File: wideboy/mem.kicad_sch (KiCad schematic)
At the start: 9 parts, among them U10 LH28F320BJE-PTTL90, U11 µPD45128163G5-A75-9Jf, U9 XC17S20LPC

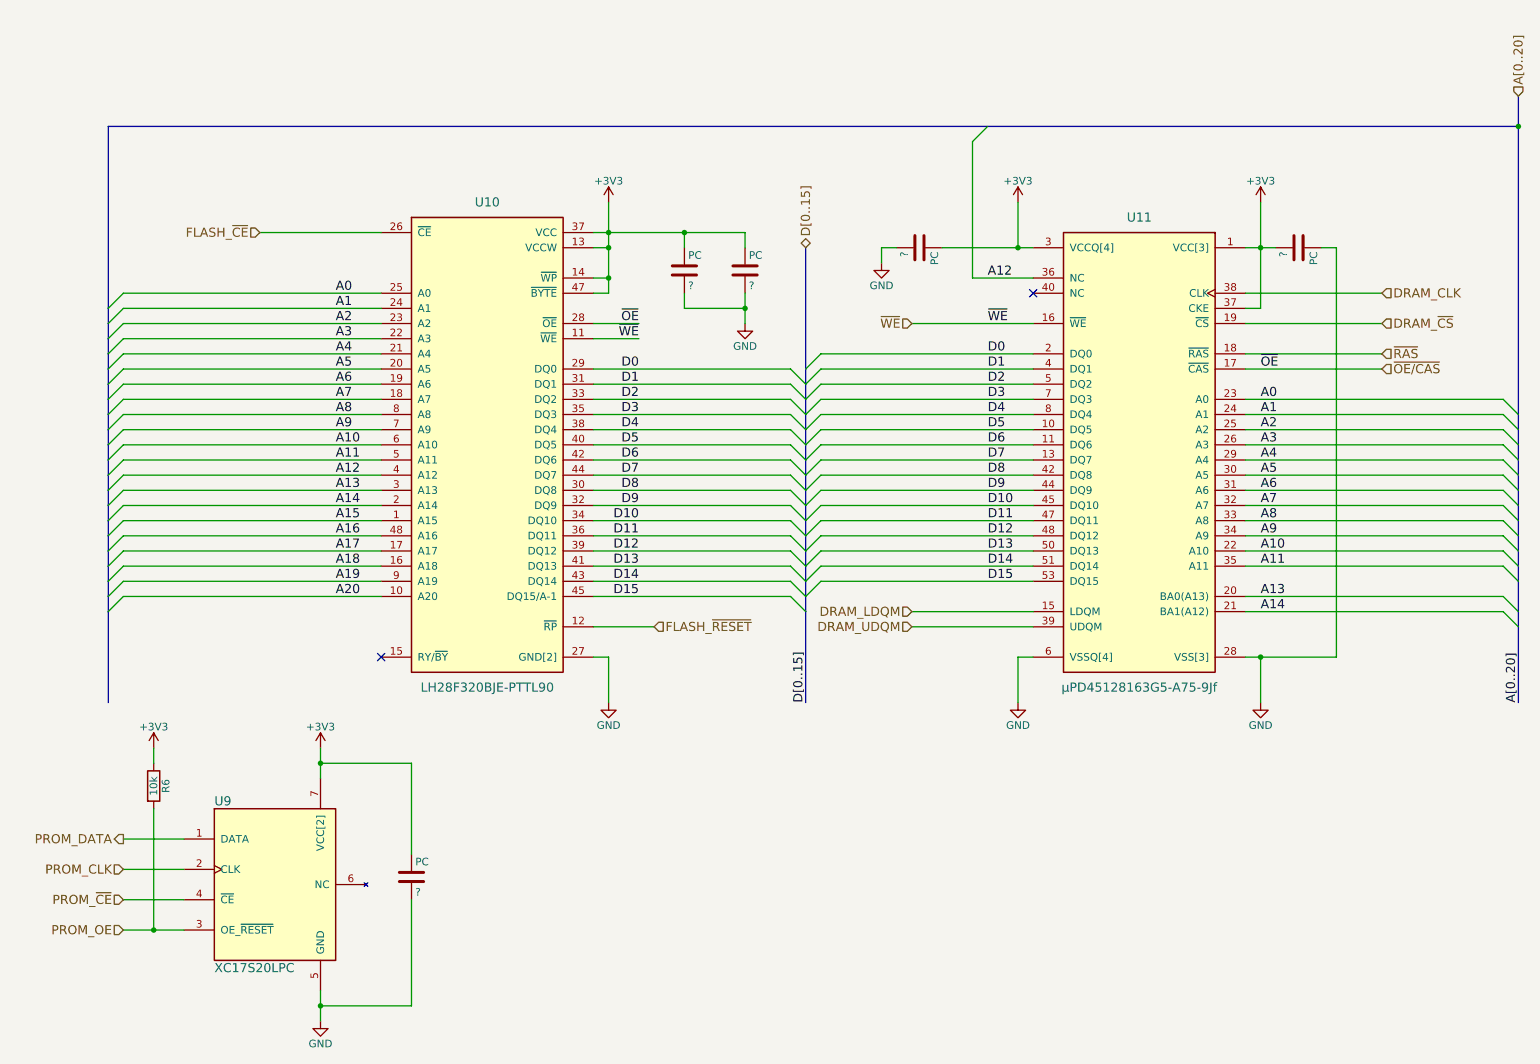
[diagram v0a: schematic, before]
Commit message: Add values for capacitors and diodes
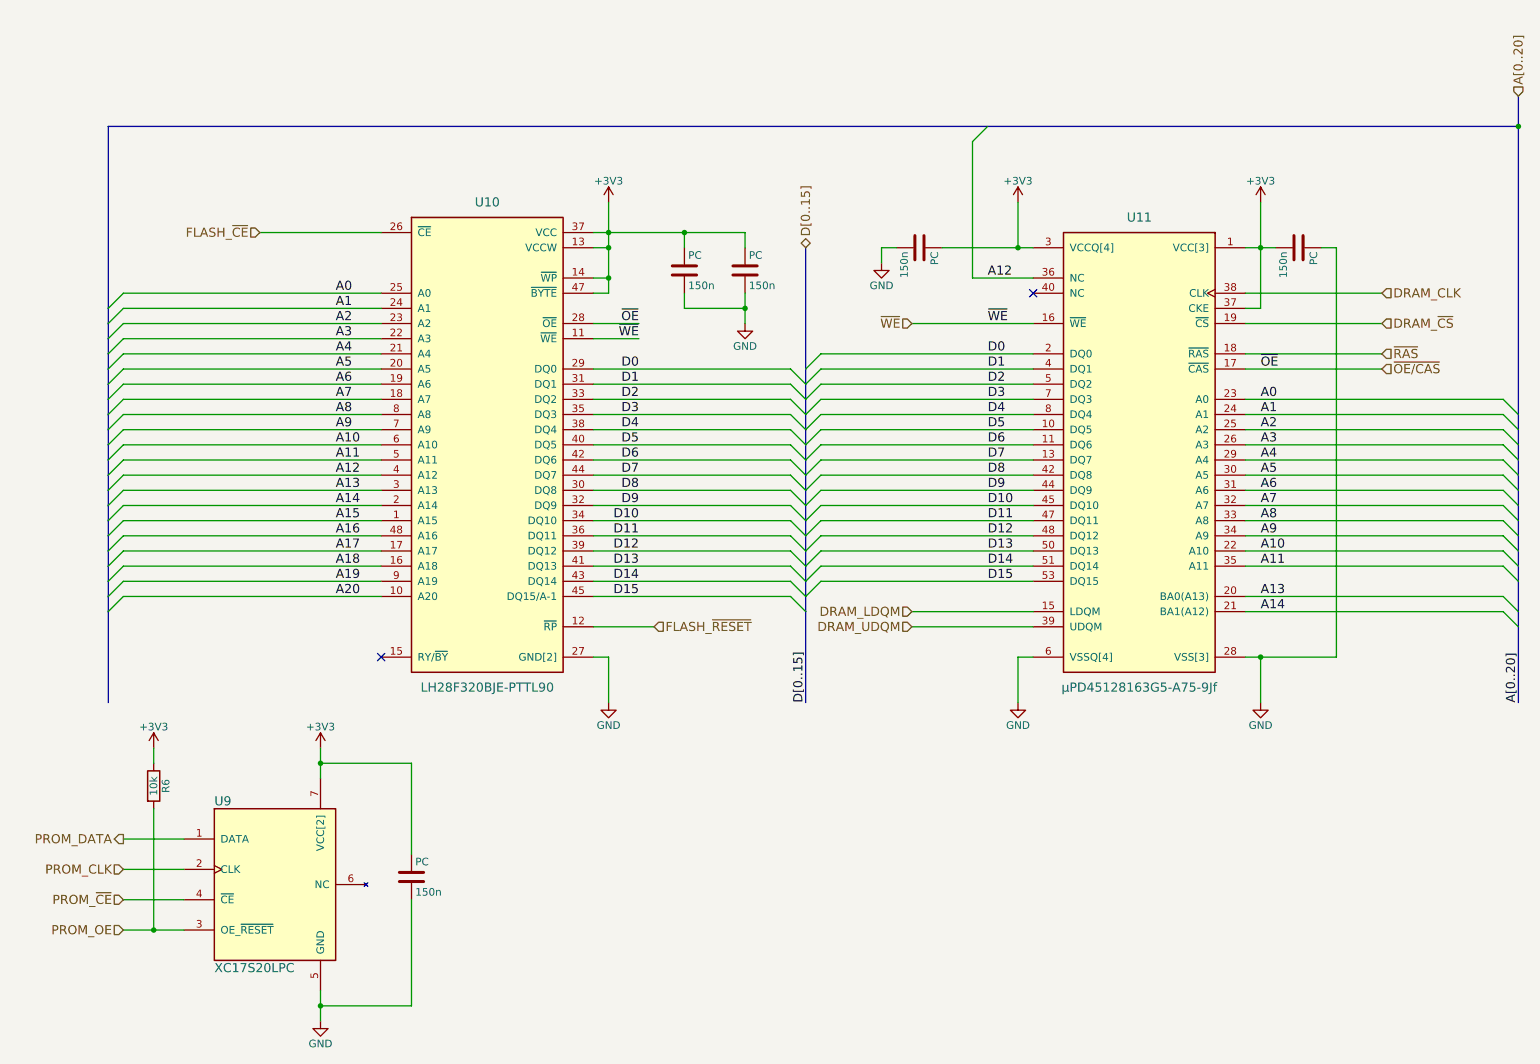
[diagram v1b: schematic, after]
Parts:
- PC: value ? -> 150n
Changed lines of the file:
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@@
 	(title_block
 		(title "Wide-Boy64 AGB")
-		(date "2024-06-20")
-		(rev "2")
+		(date "2024-09-22")
+		(rev "3")
 		(company "CC-BY-SA-4.0 Michael Singer")
 		(comment 1 "https://github.com/msinger/wideboy/")
@@
 			)
 		)
-		(property "Value" "?"
+		(property "Value" "150n"
 			(at 86.995 168.91 0)
 			(effects
@@
 			)
 		)
-		(property "Value" "?"
+		(property "Value" "150n"
 			(at 132.715 67.31 0)
 			(effects
@@
 			)
 		)
-		(property "Value" "?"
+		(property "Value" "150n"
 			(at 142.875 67.31 0)
 			(effects
@@
 			)
 		)
-		(property "Value" "?"
+		(property "Value" "150n"
 			(at 168.91 61.595 0)
 			(effects
@@
 			)
 		)
-		(property "Value" "?"
+		(property "Value" "150n"
 			(at 232.41 61.595 0)
 			(effects
